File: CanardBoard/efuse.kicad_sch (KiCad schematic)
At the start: 20 parts, among them J3 Screw_Terminal_01x02, Q1 Q_NMOS, U2 TPS25983

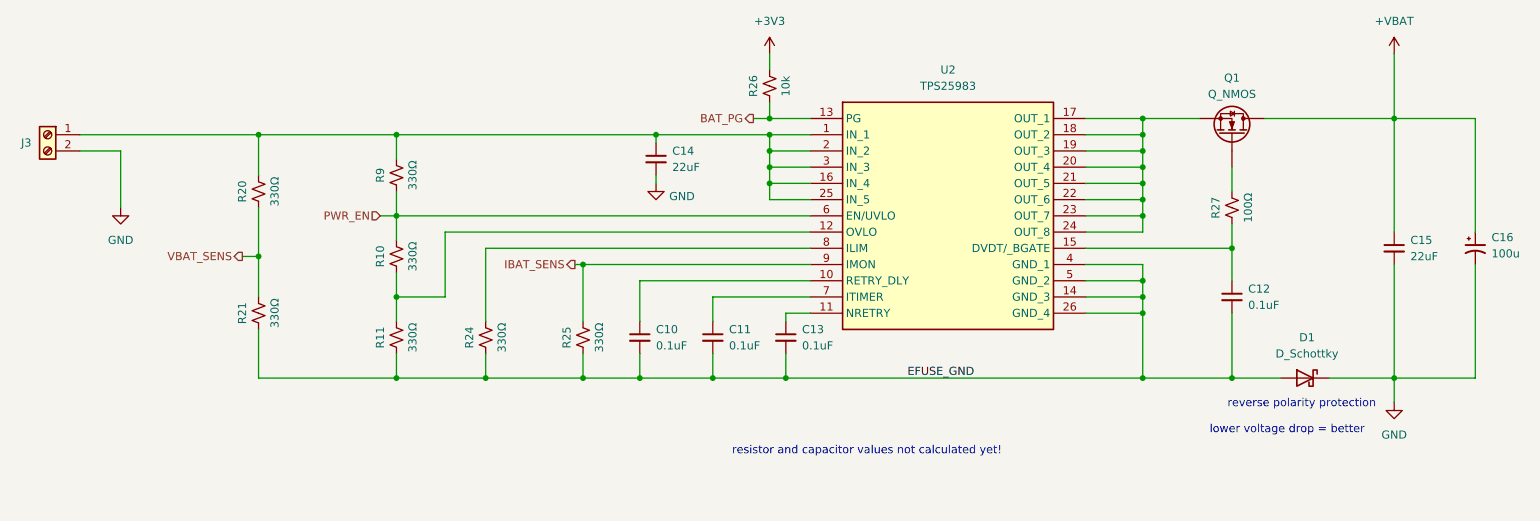
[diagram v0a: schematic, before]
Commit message: make project symbols and footprints
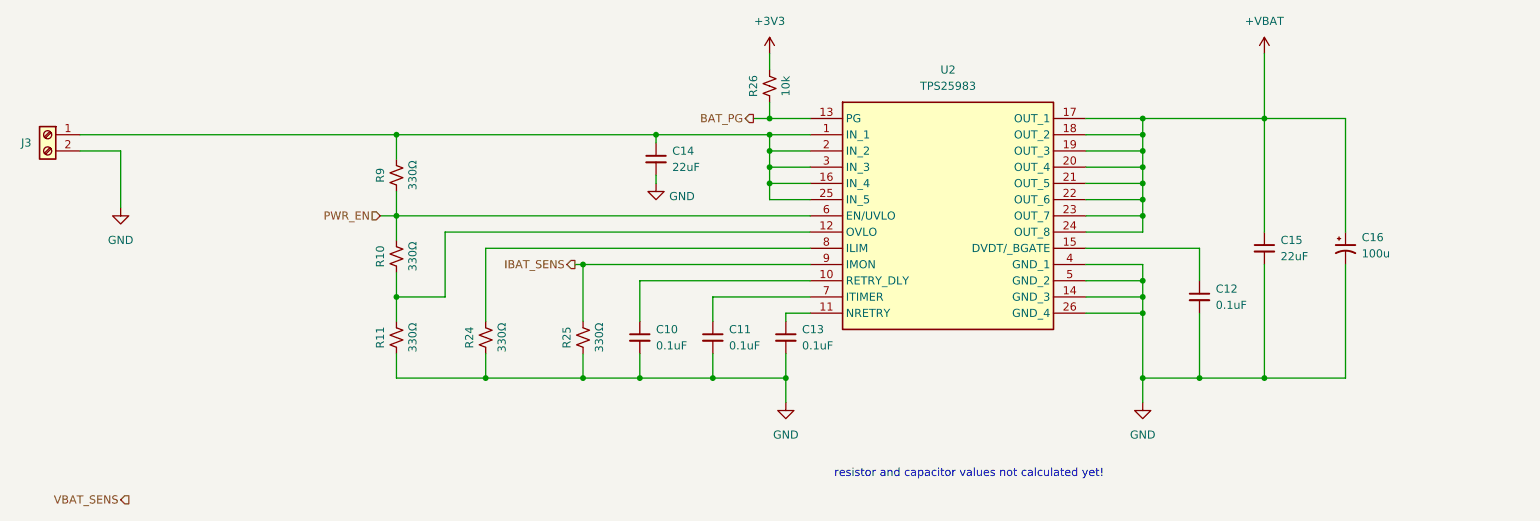
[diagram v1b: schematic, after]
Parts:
- removed D1: D_Schottky, symbol Device:D_Schottky
- removed Q1: Q_NMOS, symbol Device:Q_NMOS
- removed R20, R21: 330Ω, Resistor_SMD:R_0805_2012Metric_Pad1.20x1.40mm_HandSolder, symbol Device_Custom:R_Small_US
- removed R27: 100Ω, Resistor_SMD:R_0805_2012Metric_Pad1.20x1.40mm_HandSolder, symbol Device_Custom:R_Small_US
- U2: symbol canhw:TPS25983 -> canardboard:TPS25983
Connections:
- net EFUSE_GND is gone; now on net GND: C10.2, C11.2, C12.2, C13.2, R11.2, R24.2, R25.2, U2.14 (GND_3), U2.26 (GND_4), U2.4 (GND_1), U2.5 (GND_2)
- net +VBAT: now also U2.17 (OUT_1), U2.18 (OUT_2), U2.19 (OUT_3), U2.20 (OUT_4), U2.21 (OUT_5), U2.22 (OUT_6), U2.23 (OUT_7), U2.24 (OUT_8)
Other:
- note removed: "lower voltage drop = better"
- note removed: "reverse polarity protection"
- moved on the sheet: C12, C15, C16
